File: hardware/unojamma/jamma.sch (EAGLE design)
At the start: 33 parts, among them T1 2N3904, T2 2N3904, T3 2N3904, X1 53048-09

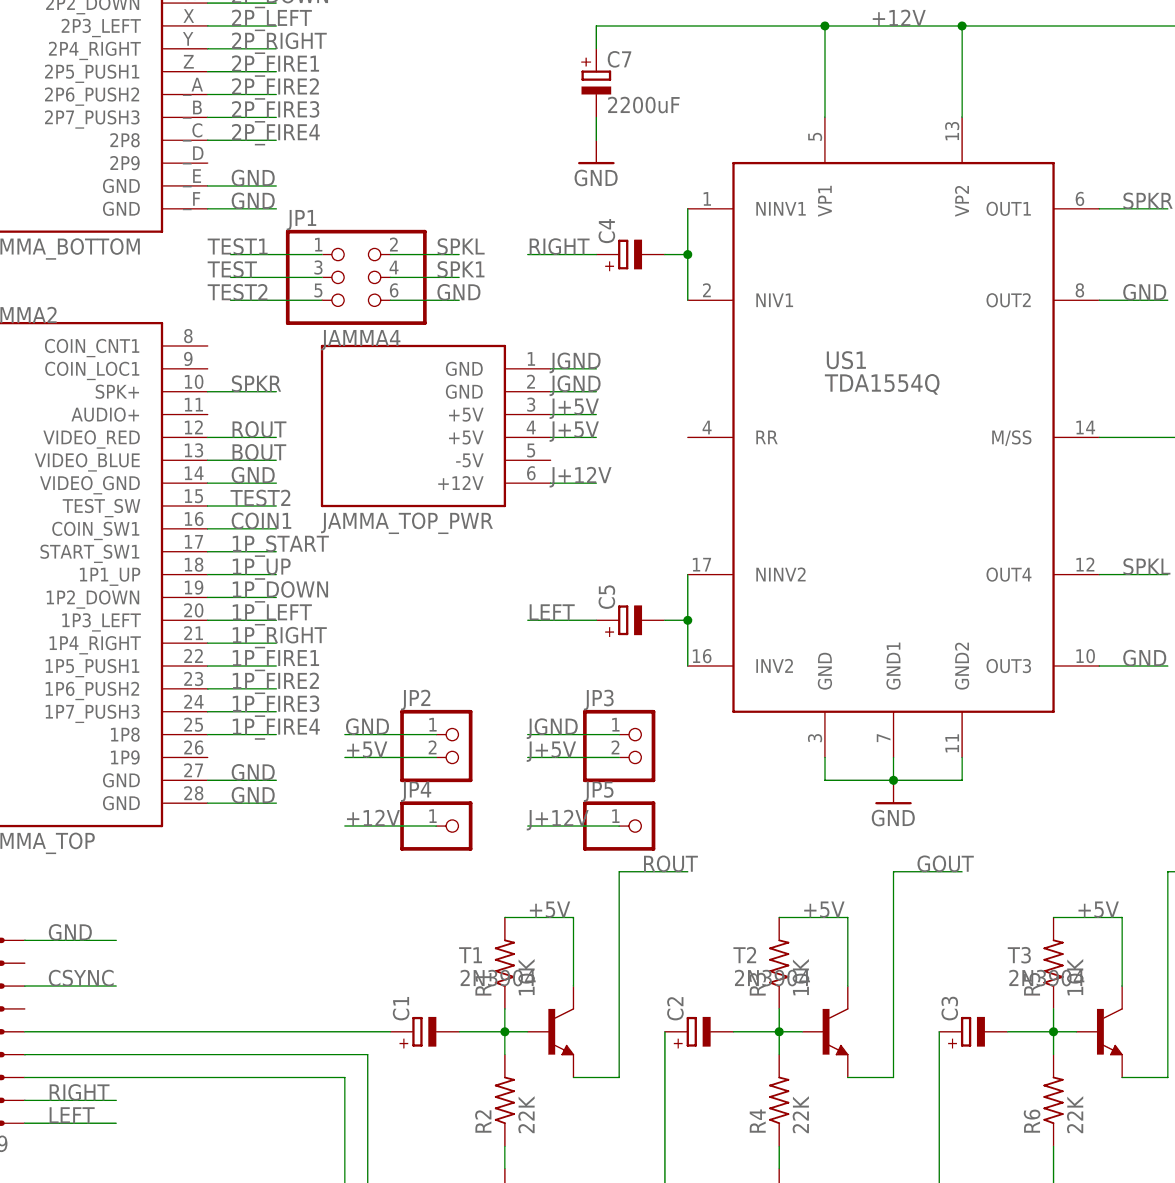
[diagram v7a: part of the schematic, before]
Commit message: Añado potenciómetros
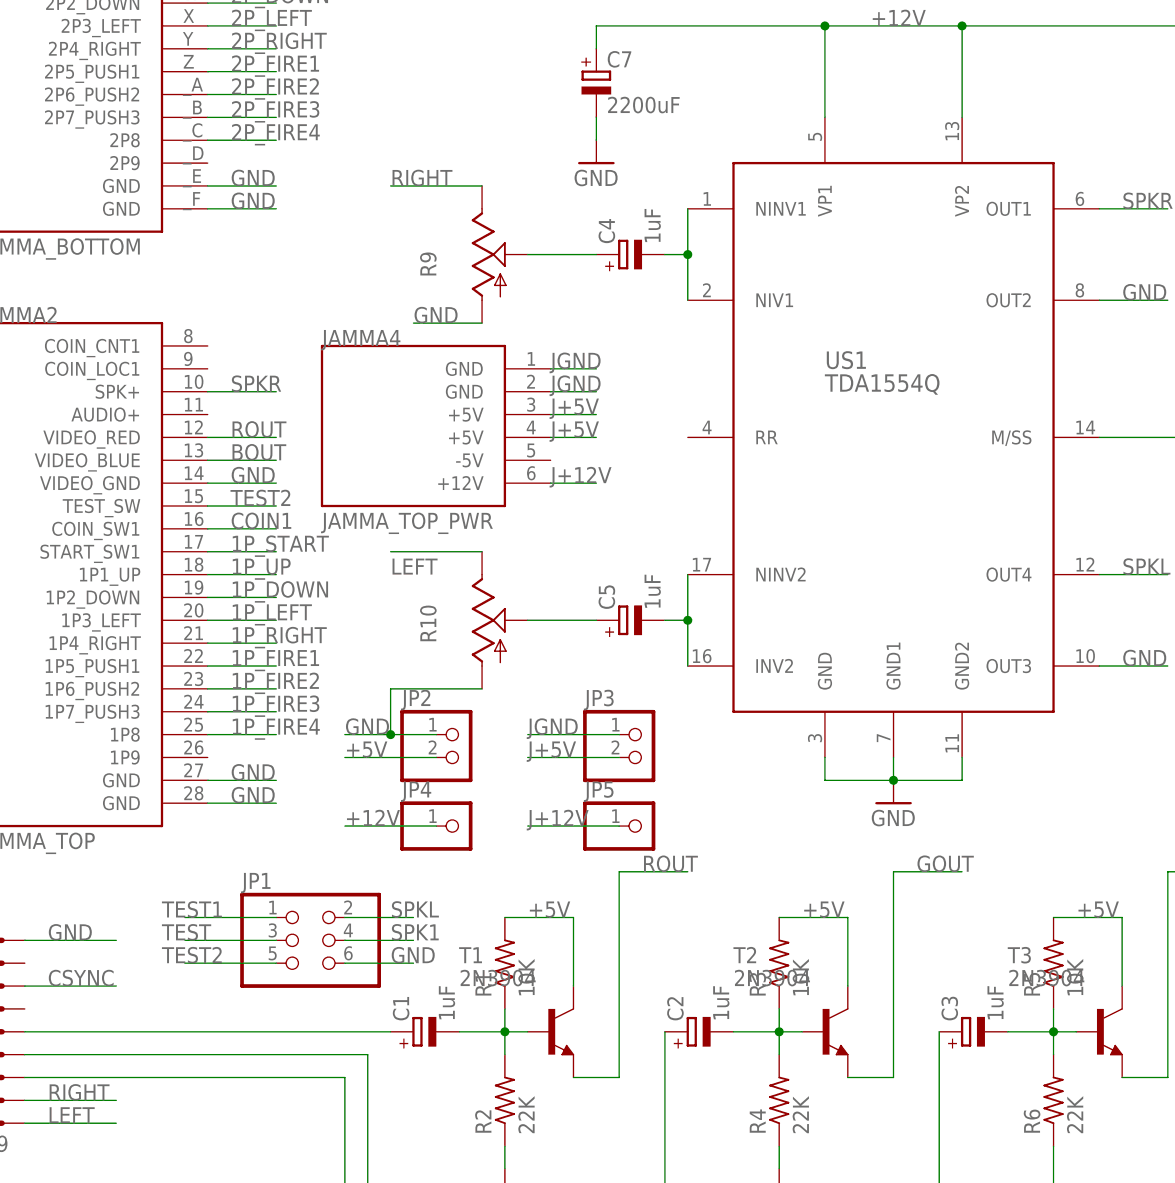
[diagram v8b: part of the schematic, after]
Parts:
- added R10, R9: (no value), pot:TRIM_US-CA6V
- C1, C2, C3, C4, C5: value (none) -> 1uF
- C6: device rcl:CPOL-EUE7.5-16 -> rcl:CPOL-EUE5-5
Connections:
- new net N$3: C5.+, R10.S
- new net N$9: C4.+, R9.S
- net GND: now also R10.A, R9.A
- net LEFT: now also R10.E; no longer C5.+
- net RIGHT: now also R9.E; no longer C4.+
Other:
- moved on the sheet: JP1
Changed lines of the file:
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@@
 <part name="T2" library="transistor" deviceset="2N3904" device=""/>
 <part name="T3" library="transistor" deviceset="2N3904" device=""/>
-<part name="C1" library="rcl" deviceset="CPOL-EU" device="E2-5"/>
-<part name="C2" library="rcl" deviceset="CPOL-EU" device="E2-5"/>
-<part name="C3" library="rcl" deviceset="CPOL-EU" device="E2-5"/>
+<part name="C1" library="rcl" deviceset="CPOL-EU" device="E2-5" value="1uF"/>
+<part name="C2" library="rcl" deviceset="CPOL-EU" device="E2-5" value="1uF"/>
+<part name="C3" library="rcl" deviceset="CPOL-EU" device="E2-5" value="1uF"/>
 <part name="US1" library="PowerAmplifier" deviceset="TDA1554" device="Q"/>
-<part name="C4" library="rcl" deviceset="CPOL-EU" device="E2-5"/>
-<part name="C5" library="rcl" deviceset="CPOL-EU" device="E2-5"/>
-<part name="C6" library="rcl" deviceset="CPOL-EU" device="E7.5-16" value="47uF"/>
+<part name="C4" library="rcl" deviceset="CPOL-EU" device="E2-5" value="1uF"/>
+<part name="C5" library="rcl" deviceset="CPOL-EU" device="E2-5" value="1uF"/>
+<part name="C6" library="rcl" deviceset="CPOL-EU" device="E5-5" value="47uF"/>
 <part name="C7" library="rcl" deviceset="CPOL-EU" device="E5-10.5" value="2200uF"/>
 <part name="GND4" library="supply1" deviceset="GND" device=""/>
@@
 <part name="SW1" library="special" deviceset="SW_DIP-8" device=""/>
 <part name="GND8" library="supply1" deviceset="GND" device=""/>
+<part name="R9" library="pot" deviceset="TRIM_US-" device="CA6V"/>
+<part name="R10" library="pot" deviceset="TRIM_US-" device="CA6V"/>
 </parts>
 <sheets>
@@
 </instance>
 <instance part="R8" gate="G$1" x="139.7" y="88.9" rot="R90"/>
-<instance part="JP1" gate="A" x="43.18" y="99.06"/>
+<instance part="JP1" gate="A" x="38.1" y="25.4"/>
 <instance part="GND7" gate="1" x="104.14" y="40.64" smashed="yes">
 <attribute name="VALUE" x="101.6" y="38.1" size="1.778" layer="96"/>
@@
 <attribute name="VALUE" x="139.7" y="-5.08" size="1.778" layer="96"/>
 </instance>
+<instance part="R9" gate="G$1" x="58.42" y="101.6"/>
+<instance part="R10" gate="G$1" x="58.42" y="60.96"/>
 </instances>
 <busses>
@@
 <segment>
 <pinref part="JP1" gate="A" pin="6"/>
-<wire x1="48.26" y1="96.52" x2="55.88" y2="96.52" width="0.1524" layer="91"/>
-<label x="53.34" y="96.52" size="1.778" layer="95"/>
+<wire x1="43.18" y1="22.86" x2="50.8" y2="22.86" width="0.1524" layer="91"/>
+<label x="48.26" y="22.86" size="1.778" layer="95"/>
 </segment>
 <segment>
@@
 <segment>
 <pinref part="JP2" gate="G$1" pin="1"/>
-<wire x1="53.34" y1="48.26" x2="43.18" y2="48.26" width="0.1524" layer="91"/>
+<wire x1="53.34" y1="48.26" x2="48.26" y2="48.26" width="0.1524" layer="91"/>
 <label x="43.18" y="48.26" size="1.778" layer="95"/>
+<pinref part="R10" gate="G$1" pin="A"/>
+<wire x1="48.26" y1="48.26" x2="43.18" y2="48.26" width="0.1524" layer="91"/>
+<wire x1="58.42" y1="53.34" x2="48.26" y2="53.34" width="0.1524" layer="91"/>
+<wire x1="48.26" y1="53.34" x2="48.26" y2="48.26" width="0.1524" layer="91"/>
+<junction x="48.26" y="48.26"/>
 </segment>
 <segment>
@@
 <junction x="142.24" y="2.54"/>
 </segment>
+<segment>
+<pinref part="R9" gate="G$1" pin="A"/>
+<wire x1="58.42" y1="93.98" x2="50.8" y2="93.98" width="0.1524" layer="91"/>
+<label x="50.8" y="93.98" size="1.778" layer="95"/>
+</segment>
 </net>
 <net name="+5V" class="1">
@@
 </segment>
 <segment>
-<pinref part="C5" gate="G$1" pin="+"/>
-<wire x1="71.12" y1="60.96" x2="63.5" y2="60.96" width="0.1524" layer="91"/>
-<label x="63.5" y="60.96" size="1.778" layer="95"/>
+<pinref part="R10" gate="G$1" pin="E"/>
+<wire x1="58.42" y1="68.58" x2="48.26" y2="68.58" width="0.1524" layer="91"/>
+<label x="48.26" y="66.04" size="1.778" layer="95"/>
 </segment>
 </net>
@@
 </segment>
 <segment>
-<pinref part="C4" gate="G$1" pin="+"/>
-<wire x1="71.12" y1="101.6" x2="63.5" y2="101.6" width="0.1524" layer="91"/>
-<label x="63.5" y="101.6" size="1.778" layer="95"/>
+<pinref part="R9" gate="G$1" pin="E"/>
+<wire x1="58.42" y1="109.22" x2="48.26" y2="109.22" width="0.1524" layer="91"/>
+<label x="48.26" y="109.22" size="1.778" layer="95"/>
 </segment>
 </net>
@@
 <segment>
 <pinref part="JP1" gate="A" pin="5"/>
-<label x="27.94" y="96.52" size="1.778" layer="95"/>
-<wire x1="40.64" y1="96.52" x2="30.48" y2="96.52" width="0.1524" layer="91"/>
+<label x="22.86" y="22.86" size="1.778" layer="95"/>
+<wire x1="35.56" y1="22.86" x2="25.4" y2="22.86" width="0.1524" layer="91"/>
 </segment>
 </net>
@@
 <segment>
 <pinref part="JP1" gate="A" pin="2"/>
-<wire x1="48.26" y1="101.6" x2="55.88" y2="101.6" width="0.1524" layer="91"/>
-<label x="53.34" y="101.6" size="1.778" layer="95"/>
+<wire x1="43.18" y1="27.94" x2="50.8" y2="27.94" width="0.1524" layer="91"/>
+<label x="48.26" y="27.94" size="1.778" layer="95"/>
 </segment>
 </net>
@@
 <segment>
 <pinref part="JP1" gate="A" pin="1"/>
-<label x="27.94" y="101.6" size="1.778" layer="95"/>
-<wire x1="40.64" y1="101.6" x2="30.48" y2="101.6" width="0.1524" layer="91"/>
+<label x="22.86" y="27.94" size="1.778" layer="95"/>
+<wire x1="35.56" y1="27.94" x2="25.4" y2="27.94" width="0.1524" layer="91"/>
 </segment>
 </net>
@@
 <segment>
 <pinref part="JP1" gate="A" pin="4"/>
-<wire x1="48.26" y1="99.06" x2="55.88" y2="99.06" width="0.1524" layer="91"/>
-<label x="53.34" y="99.06" size="1.778" layer="95"/>
+<wire x1="43.18" y1="25.4" x2="50.8" y2="25.4" width="0.1524" layer="91"/>
+<label x="48.26" y="25.4" size="1.778" layer="95"/>
 </segment>
 </net>
@@
 <segment>
 <pinref part="JP1" gate="A" pin="3"/>
-<label x="27.94" y="99.06" size="1.778" layer="95"/>
-<wire x1="40.64" y1="99.06" x2="30.48" y2="99.06" width="0.1524" layer="91"/>
+<label x="22.86" y="25.4" size="1.778" layer="95"/>
+<wire x1="35.56" y1="25.4" x2="25.4" y2="25.4" width="0.1524" layer="91"/>
 </segment>
 <segment>
@@
 </segment>
 </net>
+<net name="N$3" class="0">
+<segment>
+<pinref part="R10" gate="G$1" pin="S"/>
+<pinref part="C5" gate="G$1" pin="+"/>
+<wire x1="63.5" y1="60.96" x2="71.12" y2="60.96" width="0.1524" layer="91"/>
+</segment>
+</net>
+<net name="N$9" class="0">
+<segment>
+<pinref part="R9" gate="G$1" pin="S"/>
+<pinref part="C4" gate="G$1" pin="+"/>
+<wire x1="63.5" y1="101.6" x2="71.12" y2="101.6" width="0.1524" layer="91"/>
+</segment>
+</net>
